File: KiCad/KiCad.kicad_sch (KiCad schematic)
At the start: 16 parts, among them M1 Servo (SG90), U1 ESP32-DEVKITC, U2 microSD-DIP-KIT

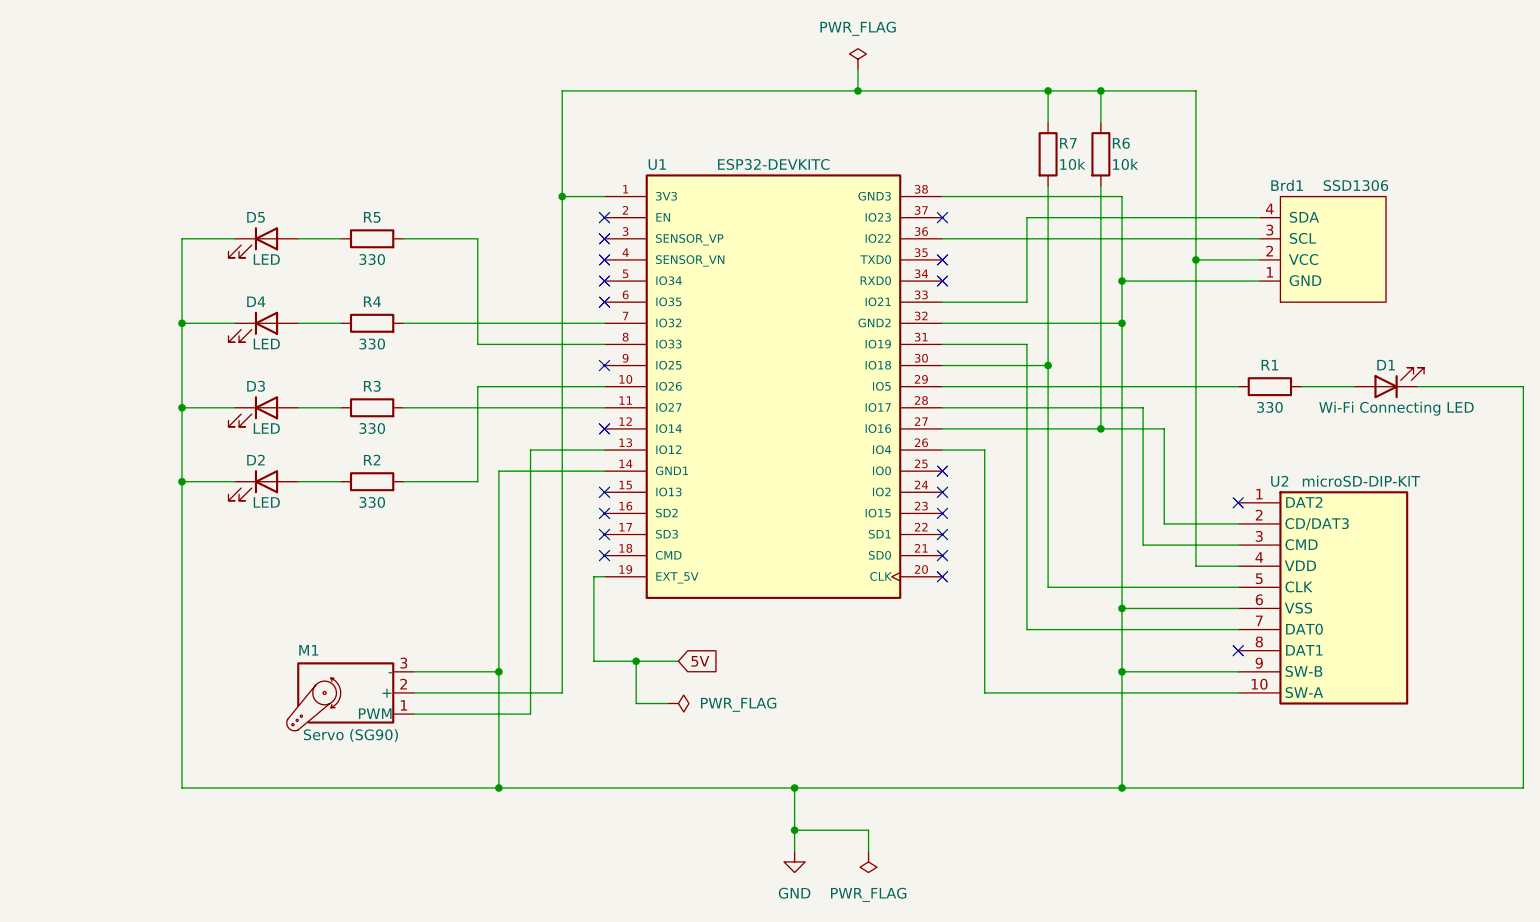
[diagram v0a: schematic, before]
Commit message: モーターコントロールを追加
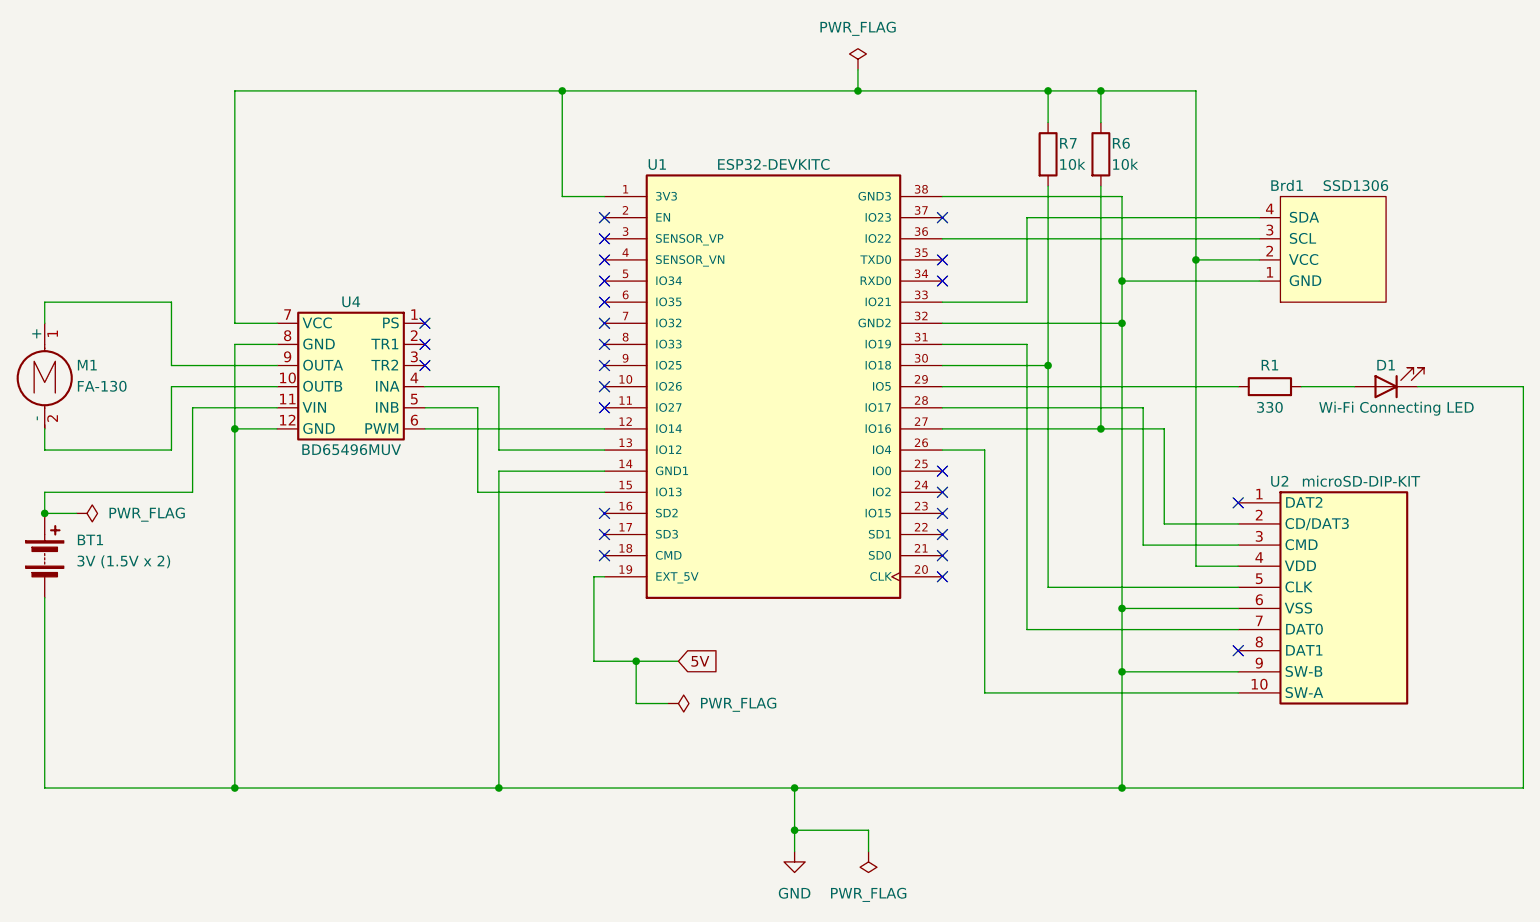
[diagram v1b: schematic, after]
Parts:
- removed D2, D3, D4, D5: LED, LED_THT:LED_D5.0mm, symbol Device:LED
- removed M1: Servo (SG90), Connector_PinHeader_2.54mm:PinHeader_1x03_P2.54mm_Horizontal, symbol Motor:Motor_Servo
- removed R2, R3, R4, R5: 330, Resistor_THT:R_Axial_DIN0204_L3.6mm_D1.6mm_P5.08mm_Horizontal, symbol Device:R
- added BT1: 3V (1.5V x 2), symbol Device:Battery
- added M1: FA-130, symbol Motor:Motor_DC
- added U4: BD65496MUV, symbol SWITCH_SCIENCE_Library:BD65496MUV_Driver
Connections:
- net GND: now also BT1.2 (-), U4.12 (GND), U4.8 (GND)
- net at Brd1.2 (VCC), R6.1, R7.1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: now also U4.7 (VCC)
- net at U1.13 (IO12): now also U4.4 (INA)
- net at U1.12 (IO14): now also U4.6 (PWM)
- net at U1.15 (IO13): now also U4.5 (INB)
- new net: M1.1 (+), U4.9 (OUTA)
- new net: M1.2 (-), U4.10 (OUTB)
- new net: BT1.1 (+), U4.11 (VIN)
- no-connect marks 22 -> 27
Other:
- title: Wi-Fiコントロールベース -> モーターコントロールサンプル

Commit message: 修正
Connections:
- net at Brd1.2 (VCC), R6.1, R7.1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: now also U4.1 (PS), U4.6 (PWM)
- net at U1.12 (IO14): no longer U4.6 (PWM)
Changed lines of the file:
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@@
   (junction (at 139.7 144.78) (diameter 0) (color 0 0 0 0)
   )
+  (junction (at 97.79 88.9) (diameter 0) (color 0 0 0 0)
+  )
   (junction (at 111.76 60.96) (diameter 0) (color 0 0 0 0)
   )
@@
   (junction (at 120.65 129.54) (diameter 0) (color 0 0 0 0)
   )
+  (junction (at 72.39 83.82) (diameter 0) (color 0 0 0 0)
+  )
   (junction (at 104.14 144.78) (diameter 0) (color 0 0 0 0)
   )
-  (no_connect (at 95.25 88.9))
   (no_connect (at 157.48 109.22))
   (no_connect (at 116.84 91.44))
   (no_connect (at 157.48 119.38))
+  (no_connect (at 116.84 101.6))
   (no_connect (at 193.04 128.27))
   (no_connect (at 95.25 91.44))
@@
     (stroke (width 0) (type default))
   )
-  (wire (pts (xy 72.39 60.96) (xy 72.39 88.9))
+  (wire (pts (xy 72.39 60.96) (xy 72.39 83.82))
     (stroke (width 0) (type default))
   )
@@
     (stroke (width 0) (type default))
   )
+  (wire (pts (xy 97.79 88.9) (xy 97.79 83.82))
+    (stroke (width 0) (type default))
+  )
   (wire (pts (xy 72.39 88.9) (xy 77.47 88.9))
     (stroke (width 0) (type default))
@@
     (stroke (width 0) (type default))
   )
+  (wire (pts (xy 95.25 88.9) (xy 97.79 88.9))
+    (stroke (width 0) (type default))
+  )
   (wire (pts (xy 157.48 88.9) (xy 179.07 88.9))
     (stroke (width 0) (type default))
@@
     (stroke (width 0) (type default))
   )
+  (wire (pts (xy 72.39 83.82) (xy 97.79 83.82))
+    (stroke (width 0) (type default))
+  )
+  (wire (pts (xy 97.79 101.6) (xy 97.79 88.9))
+    (stroke (width 0) (type default))
+  )
   (wire (pts (xy 101.6 109.22) (xy 101.6 99.06))
     (stroke (width 0) (type default))
@@
     (stroke (width 0) (type default))
   )
-  (wire (pts (xy 95.25 101.6) (xy 116.84 101.6))
-    (stroke (width 0) (type default))
-  )
   (wire (pts (xy 162.56 133.35) (xy 162.56 104.14))
     (stroke (width 0) (type default))
@@
     (stroke (width 0) (type default))
   )
+  (wire (pts (xy 72.39 83.82) (xy 72.39 88.9))
+    (stroke (width 0) (type default))
+  )
   (wire (pts (xy 170.18 60.96) (xy 176.53 60.96))
     (stroke (width 0) (type default))
@@
     (stroke (width 0) (type default))
   )
+  (wire (pts (xy 95.25 101.6) (xy 97.79 101.6))
+    (stroke (width 0) (type default))
+  )

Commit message: KiCadの回路図追加
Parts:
- BT1, M1: footprint (none) -> Connector_PinHeader_1.27mm:PinHeader_1x02_P1.27mm_Vertical
- U4: footprint (none) -> SWITCH_SCIENCE:BD65496MUV
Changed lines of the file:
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@@
       (effects (font (size 1.27 1.27)) (justify left))
     )
-    (property "Footprint" "" (at 49.53 96.266 0)
+    (property "Footprint" "Connector_PinHeader_1.27mm:PinHeader_1x02_P1.27mm_Vertical" (at 49.53 96.266 0)
       (effects (font (size 1.27 1.27)) hide)
     )
@@
       (effects (font (size 1.27 1.27)))
     )
-    (property "Footprint" "" (at 86.36 86.36 0)
+    (property "Footprint" "SWITCH_SCIENCE:BD65496MUV" (at 86.36 86.36 0)
       (effects (font (size 1.27 1.27)) hide)
     )
@@
       (effects (font (size 1.27 1.27)) (justify left))
     )
-    (property "Footprint" "" (at 49.53 115.316 90)
-      (effects (font (size 1.27 1.27)) hide)
-    )
+    (property "Footprint" "Connector_PinHeader_1.27mm:PinHeader_1x02_P1.27mm_Vertical" (at 49.53 115.316 90)
+      (effects (font (size 1.27 1.27)) hide)
+    )
